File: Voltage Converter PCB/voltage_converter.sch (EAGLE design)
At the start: 11 parts

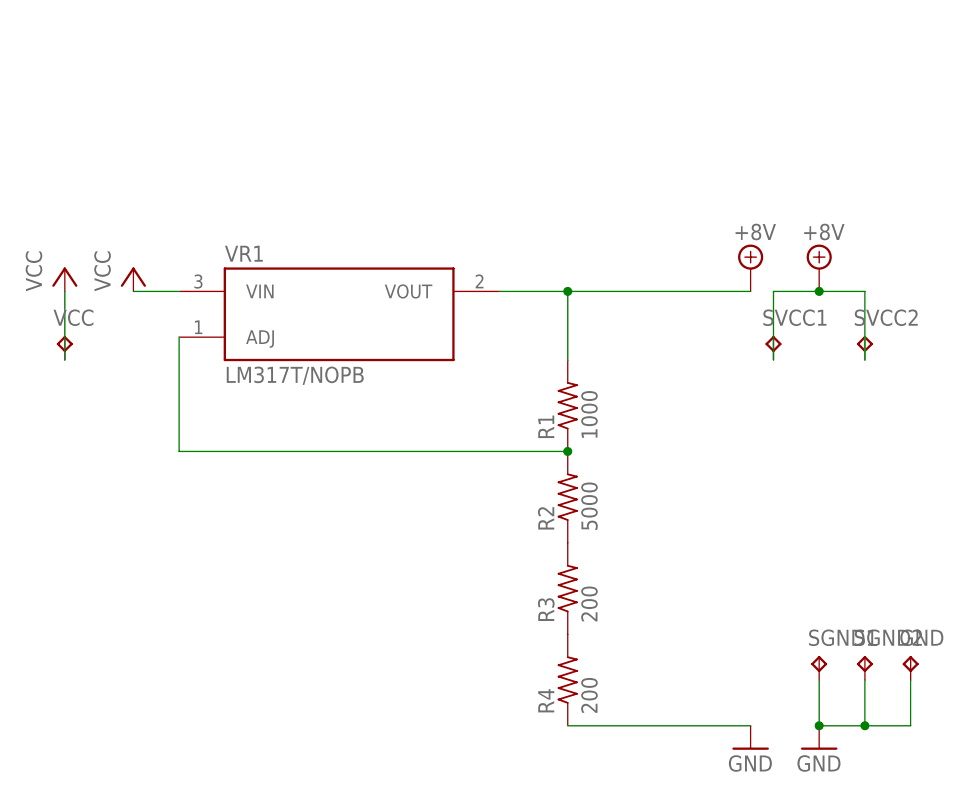
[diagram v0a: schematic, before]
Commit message: consolidated facial detection, added battery_basket, new voltage converter board
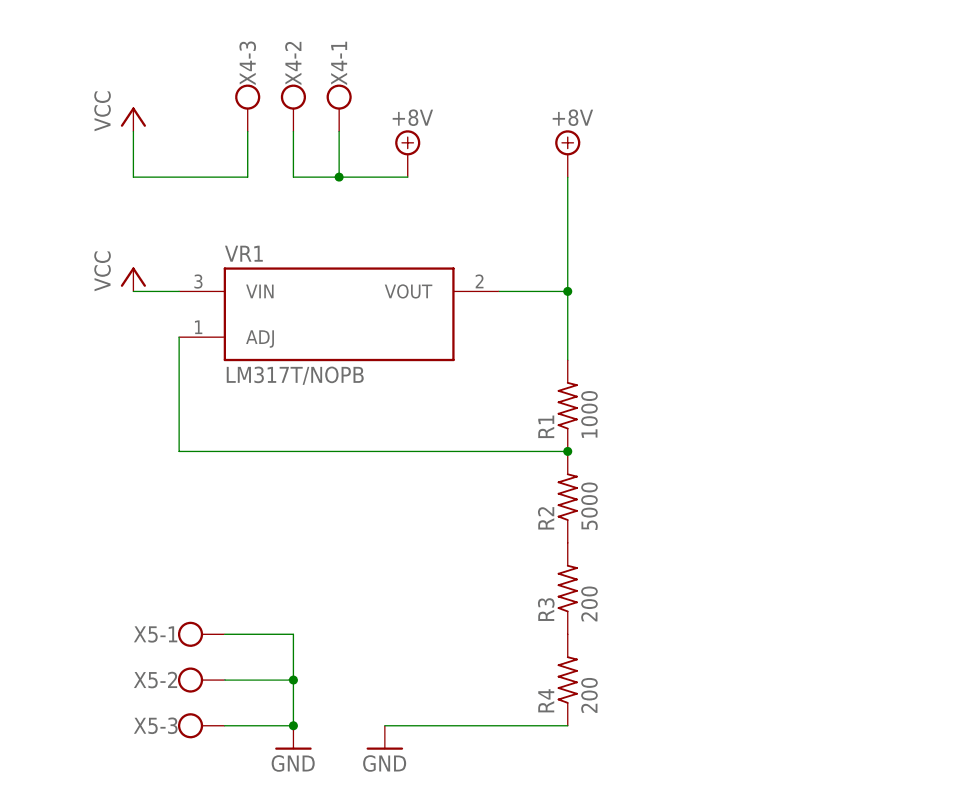
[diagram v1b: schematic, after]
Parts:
- removed GND, SGND1, SGND2, SVCC1, SVCC2, VCC: TPPAD1-13, testpad:TPPAD1-13
- added X4, X5: (no value), con-wago-500:W237-103
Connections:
- net +8V: now also X4-1.KL, X4-2.KL; no longer SVCC1.TP, SVCC2.TP
- net GND: now also X5-1.KL, X5-2.KL, X5-3.KL; no longer GND.TP, SGND1.TP, SGND2.TP
- net VCC: now also X4-3.KL; no longer VCC.TP
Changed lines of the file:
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@@
 <part name="SUPPLY2" library="supply2" library_urn="urn:adsk.eagle:library:372" deviceset="+8V" device=""/>
 <part name="GND2" library="supply1" library_urn="urn:adsk.eagle:library:371" deviceset="GND" device=""/>
-<part name="SVCC1" library="testpad" library_urn="urn:adsk.eagle:library:385" deviceset="TP" device="PAD1-13" package3d_urn="urn:adsk.eagle:package:27946/1"/>
-<part name="SVCC2" library="testpad" library_urn="urn:adsk.eagle:library:385" deviceset="TP" device="PAD1-13" package3d_urn="urn:adsk.eagle:package:27946/1"/>
-<part name="SGND1" library="testpad" library_urn="urn:adsk.eagle:library:385" deviceset="TP" device="PAD1-13" package3d_urn="urn:adsk.eagle:package:27946/1"/>
-<part name="VCC" library="testpad" library_urn="urn:adsk.eagle:library:385" deviceset="TP" device="PAD1-13" package3d_urn="urn:adsk.eagle:package:27946/1"/>
 <part name="P+3" library="supply1" library_urn="urn:adsk.eagle:library:371" deviceset="VCC" device=""/>
 <part name="P+4" library="supply1" library_urn="urn:adsk.eagle:library:371" deviceset="VCC" device=""/>
-<part name="SGND2" library="testpad" library_urn="urn:adsk.eagle:library:385" deviceset="TP" device="PAD1-13" package3d_urn="urn:adsk.eagle:package:27946/1"/>
-<part name="GND" library="testpad" library_urn="urn:adsk.eagle:library:385" deviceset="TP" device="PAD1-13" package3d_urn="urn:adsk.eagle:package:27946/1"/>
 <part name="VR1" library="chmip" deviceset="LM317T/NOPB" device=""/>
+<part name="X4" library="con-wago-500" library_urn="urn:adsk.eagle:library:195" deviceset="W237-103" device="" package3d_urn="urn:adsk.eagle:package:10691/1"/>
+<part name="X5" library="con-wago-500" library_urn="urn:adsk.eagle:library:195" deviceset="W237-103" device="" package3d_urn="urn:adsk.eagle:package:10691/1"/>
 </parts>
 <sheets>
@@
 <attribute name="VALUE" x="61.722" y="26.67" size="1.778" layer="96" rot="R90"/>
 </instance>
-<instance part="GND1" gate="1" x="78.74" y="22.86" smashed="yes">
-<attribute name="VALUE" x="76.2" y="20.32" size="1.778" layer="96"/>
+<instance part="GND1" gate="1" x="38.1" y="22.86" smashed="yes">
+<attribute name="VALUE" x="35.56" y="20.32" size="1.778" layer="96"/>
 </instance>
-<instance part="SUPPLY1" gate="+8V" x="78.74" y="76.2" smashed="yes">
-<attribute name="VALUE" x="76.835" y="79.375" size="1.778" layer="96"/>
+<instance part="SUPPLY1" gate="+8V" x="58.42" y="88.9" smashed="yes">
+<attribute name="VALUE" x="56.515" y="92.075" size="1.778" layer="96"/>
 </instance>
-<instance part="SUPPLY2" gate="+8V" x="86.36" y="76.2" smashed="yes">
-<attribute name="VALUE" x="84.455" y="79.375" size="1.778" layer="96"/>
+<instance part="SUPPLY2" gate="+8V" x="40.64" y="88.9" smashed="yes">
+<attribute name="VALUE" x="38.735" y="92.075" size="1.778" layer="96"/>
 </instance>
-<instance part="GND2" gate="1" x="86.36" y="22.86" smashed="yes">
-<attribute name="VALUE" x="83.82" y="20.32" size="1.778" layer="96"/>
+<instance part="GND2" gate="1" x="27.94" y="22.86" smashed="yes">
+<attribute name="VALUE" x="25.4" y="20.32" size="1.778" layer="96"/>
 </instance>
-<instance part="SVCC1" gate="G$1" x="81.28" y="68.58" smashed="yes">
-<attribute name="NAME" x="80.01" y="69.85" size="1.778" layer="95"/>
-<attribute name="TP_SIGNAL_NAME" x="82.55" y="67.31" size="1.778" layer="97"/>
-</instance>
-<instance part="SVCC2" gate="G$1" x="91.44" y="68.58" smashed="yes">
-<attribute name="NAME" x="90.17" y="69.85" size="1.778" layer="95"/>
-<attribute name="TP_SIGNAL_NAME" x="92.71" y="67.31" size="1.778" layer="97"/>
-</instance>
-<instance part="SGND1" gate="G$1" x="86.36" y="33.02" smashed="yes">
-<attribute name="NAME" x="85.09" y="34.29" size="1.778" layer="95"/>
-<attribute name="TP_SIGNAL_NAME" x="87.63" y="31.75" size="1.778" layer="97"/>
-</instance>
-<instance part="VCC" gate="G$1" x="2.54" y="68.58" smashed="yes">
-<attribute name="NAME" x="1.27" y="69.85" size="1.778" layer="95"/>
-<attribute name="TP_SIGNAL_NAME" x="3.81" y="67.31" size="1.778" layer="97"/>
-</instance>
-<instance part="P+3" gate="VCC" x="2.54" y="76.2" smashed="yes">
-<attribute name="VALUE" x="0" y="73.66" size="1.778" layer="96" rot="R90"/>
+<instance part="P+3" gate="VCC" x="10.16" y="93.98" smashed="yes">
+<attribute name="VALUE" x="7.62" y="91.44" size="1.778" layer="96" rot="R90"/>
 </instance>
 <instance part="P+4" gate="VCC" x="10.16" y="76.2" smashed="yes">
 <attribute name="VALUE" x="7.62" y="73.66" size="1.778" layer="96" rot="R90"/>
 </instance>
-<instance part="SGND2" gate="G$1" x="91.44" y="33.02" smashed="yes">
-<attribute name="NAME" x="90.17" y="34.29" size="1.778" layer="95"/>
-<attribute name="TP_SIGNAL_NAME" x="92.71" y="31.75" size="1.778" layer="97"/>
-</instance>
-<instance part="GND" gate="G$1" x="96.52" y="33.02" smashed="yes">
-<attribute name="NAME" x="95.25" y="34.29" size="1.778" layer="95"/>
-<attribute name="TP_SIGNAL_NAME" x="97.79" y="31.75" size="1.778" layer="97"/>
-</instance>
 <instance part="VR1" gate="G$1" x="33.02" y="71.12" smashed="yes">
 <attribute name="NAME" x="20.32" y="76.962" size="1.778" layer="95"/>
 <attribute name="VALUE" x="20.32" y="65.278" size="1.778" layer="96" align="top-left"/>
+</instance>
+<instance part="X4" gate="-1" x="33.02" y="96.52" smashed="yes" rot="R270">
+<attribute name="NAME" x="33.909" y="96.52" size="1.778" layer="95" rot="R90"/>
+</instance>
+<instance part="X4" gate="-2" x="27.94" y="96.52" smashed="yes" rot="R270">
+<attribute name="NAME" x="28.829" y="96.52" size="1.778" layer="95" rot="R90"/>
+</instance>
+<instance part="X4" gate="-3" x="22.86" y="96.52" smashed="yes" rot="R270">
+<attribute name="VALUE" x="19.177" y="99.06" size="1.778" layer="96" rot="R270"/>
+<attribute name="NAME" x="23.749" y="96.52" size="1.778" layer="95" rot="R90"/>
+</instance>
+<instance part="X5" gate="-1" x="15.24" y="35.56" smashed="yes">
+<attribute name="NAME" x="15.24" y="36.449" size="1.778" layer="95" rot="R180"/>
+</instance>
+<instance part="X5" gate="-2" x="15.24" y="30.48" smashed="yes">
+<attribute name="NAME" x="15.24" y="31.369" size="1.778" layer="95" rot="R180"/>
+</instance>
+<instance part="X5" gate="-3" x="15.24" y="25.4" smashed="yes">
+<attribute name="VALUE" x="12.7" y="21.717" size="1.778" layer="96"/>
+<attribute name="NAME" x="15.24" y="26.289" size="1.778" layer="95" rot="R180"/>
 </instance>
 </instances>
@@
 <pinref part="R1" gate="G$1" pin="2"/>
 <wire x1="50.8" y1="73.66" x2="58.42" y2="73.66" width="0.1524" layer="91"/>
-<wire x1="58.42" y1="73.66" x2="78.74" y2="73.66" width="0.1524" layer="91"/>
+<wire x1="58.42" y1="73.66" x2="58.42" y2="86.36" width="0.1524" layer="91"/>
 <wire x1="58.42" y1="66.04" x2="58.42" y2="73.66" width="0.1524" layer="91"/>
 <junction x="58.42" y="73.66"/>
@@
 <segment>
 <pinref part="SUPPLY2" gate="+8V" pin="+8V"/>
-<pinref part="SVCC1" gate="G$1" pin="TP"/>
-<wire x1="86.36" y1="73.66" x2="81.28" y2="73.66" width="0.1524" layer="91"/>
-<wire x1="81.28" y1="73.66" x2="81.28" y2="66.04" width="0.1524" layer="91"/>
-<pinref part="SVCC2" gate="G$1" pin="TP"/>
-<wire x1="86.36" y1="73.66" x2="91.44" y2="73.66" width="0.1524" layer="91"/>
-<wire x1="91.44" y1="73.66" x2="91.44" y2="66.04" width="0.1524" layer="91"/>
-<junction x="86.36" y="73.66"/>
+<pinref part="X4" gate="-1" pin="KL"/>
+<wire x1="40.64" y1="86.36" x2="33.02" y2="86.36" width="0.1524" layer="91"/>
+<wire x1="33.02" y1="86.36" x2="33.02" y2="91.44" width="0.1524" layer="91"/>
+<wire x1="33.02" y1="86.36" x2="27.94" y2="86.36" width="0.1524" layer="91"/>
+<junction x="33.02" y="86.36"/>
+<pinref part="X4" gate="-2" pin="KL"/>
+<wire x1="27.94" y1="86.36" x2="27.94" y2="91.44" width="0.1524" layer="91"/>
 </segment>
 </net>
@@
 <segment>
 <pinref part="R4" gate="G$1" pin="1"/>
-<wire x1="58.42" y1="25.4" x2="78.74" y2="25.4" width="0.1524" layer="91"/>
+<wire x1="58.42" y1="25.4" x2="38.1" y2="25.4" width="0.1524" layer="91"/>
 <pinref part="GND1" gate="1" pin="GND"/>
 </segment>
 <segment>
-<pinref part="SGND1" gate="G$1" pin="TP"/>
+<pinref part="X5" gate="-3" pin="KL"/>
 <pinref part="GND2" gate="1" pin="GND"/>
-<wire x1="86.36" y1="30.48" x2="86.36" y2="25.4" width="0.1524" layer="91"/>
-<pinref part="SGND2" gate="G$1" pin="TP"/>
-<wire x1="91.44" y1="30.48" x2="91.44" y2="25.4" width="0.1524" layer="91"/>
-<wire x1="91.44" y1="25.4" x2="86.36" y2="25.4" width="0.1524" layer="91"/>
-<junction x="86.36" y="25.4"/>
-<pinref part="GND" gate="G$1" pin="TP"/>
-<wire x1="91.44" y1="25.4" x2="96.52" y2="25.4" width="0.1524" layer="91"/>
-<wire x1="96.52" y1="25.4" x2="96.52" y2="30.48" width="0.1524" layer="91"/>
-<junction x="91.44" y="25.4"/>
+<wire x1="20.32" y1="25.4" x2="27.94" y2="25.4" width="0.1524" layer="91"/>
+<pinref part="X5" gate="-2" pin="KL"/>
+<pinref part="X5" gate="-1" pin="KL"/>
+<wire x1="20.32" y1="35.56" x2="27.94" y2="35.56" width="0.1524" layer="91"/>
+<wire x1="27.94" y1="35.56" x2="27.94" y2="30.48" width="0.1524" layer="91"/>
+<junction x="27.94" y="25.4"/>
+<wire x1="27.94" y1="30.48" x2="27.94" y2="25.4" width="0.1524" layer="91"/>
+<wire x1="20.32" y1="30.48" x2="27.94" y2="30.48" width="0.1524" layer="91"/>
+<junction x="27.94" y="30.48"/>
 </segment>
 </net>
 <net name="VCC" class="0">
-<segment>
-<pinref part="VCC" gate="G$1" pin="TP"/>
-<wire x1="2.54" y1="66.04" x2="2.54" y2="73.66" width="0.1524" layer="91"/>
-<pinref part="P+3" gate="VCC" pin="VCC"/>
-</segment>
 <segment>
 <pinref part="P+4" gate="VCC" pin="VCC"/>
@@
 <wire x1="15.24" y1="73.66" x2="10.16" y2="73.66" width="0.1524" layer="91"/>
 </segment>
+<segment>
+<pinref part="P+3" gate="VCC" pin="VCC"/>
+<wire x1="10.16" y1="91.44" x2="10.16" y2="86.36" width="0.1524" layer="91"/>
+<pinref part="X4" gate="-3" pin="KL"/>
+<wire x1="10.16" y1="86.36" x2="22.86" y2="86.36" width="0.1524" layer="91"/>
+<wire x1="22.86" y1="86.36" x2="22.86" y2="91.44" width="0.1524" layer="91"/>
+</segment>
 </net>
